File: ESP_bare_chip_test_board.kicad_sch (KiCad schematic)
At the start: 0 parts

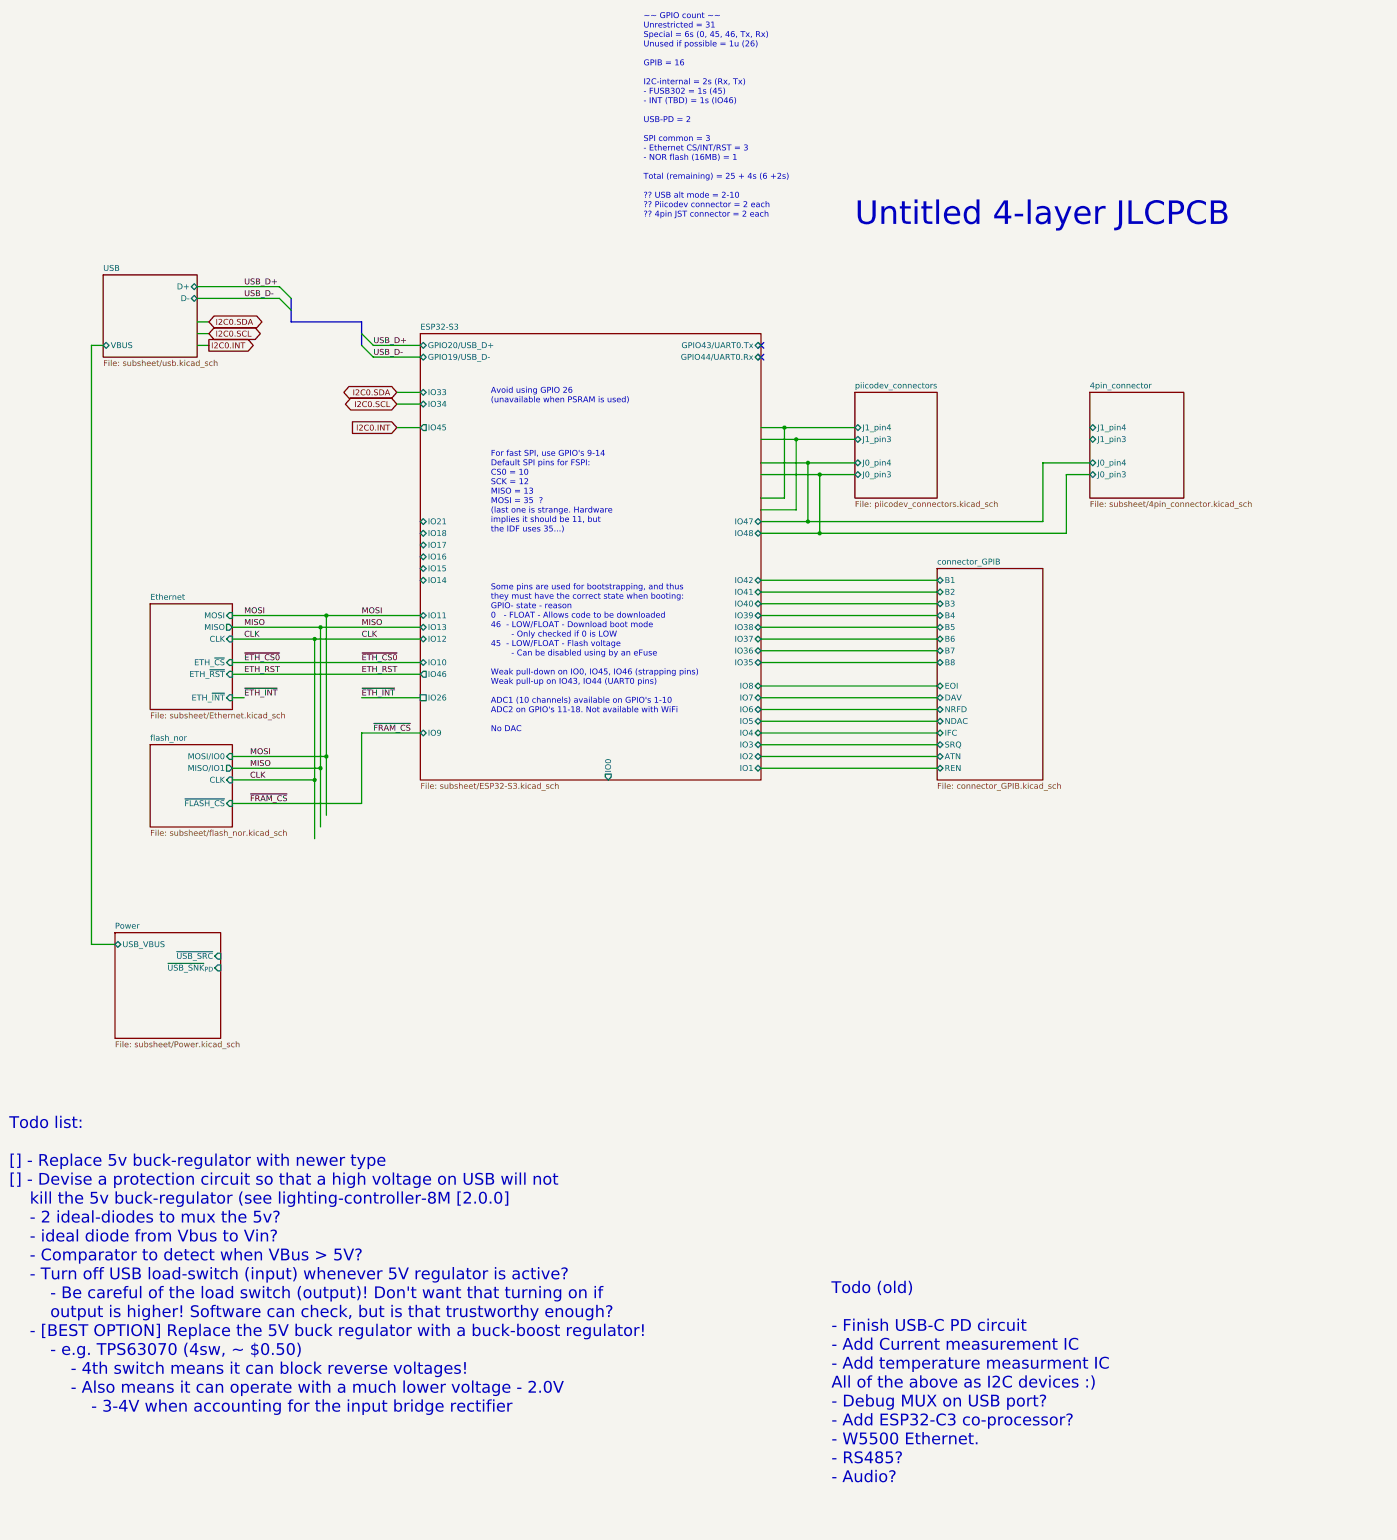
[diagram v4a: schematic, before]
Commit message: partial! Ran wires for GPIB connector
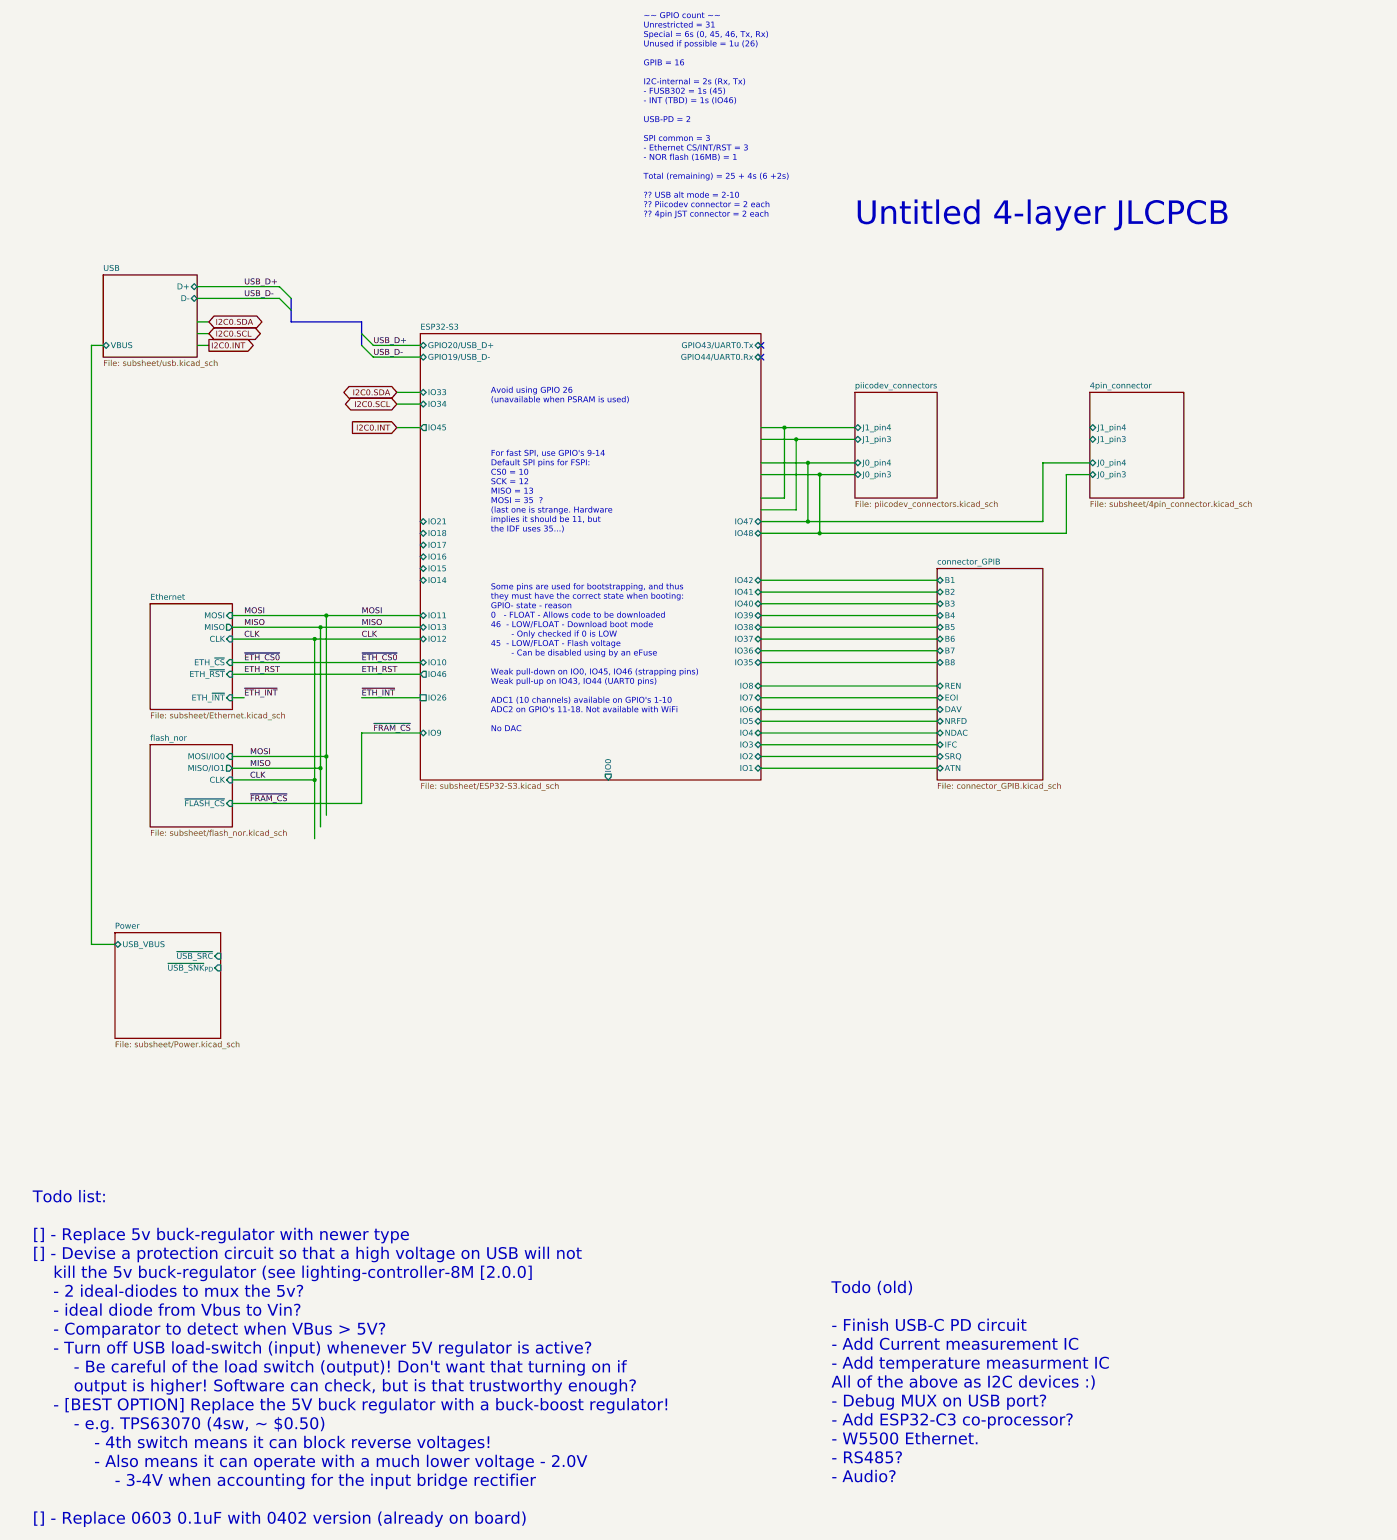
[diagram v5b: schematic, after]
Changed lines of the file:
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@@
 		)
 	)
-	(text "Todo list:\n\n[] - Replace 5v buck-regulator with newer type\n[] - Devise a protection circuit so that a high voltage on USB will not\n	kill the 5v buck-regulator (see lighting-controller-8M [2.0.0]\n	- 2 ideal-diodes to mux the 5v?\n	- ideal diode from Vbus to Vin?\n	- Comparator to detect when VBus > 5V?\n	- Turn off USB load-switch (input) whenever 5V regulator is active?\n		- Be careful of the load switch (output)! Don't want that turning on if\n		output is higher! Software can check, but is that trustworthy enough?\n	- [BEST OPTION] Replace the 5V buck regulator with a buck-boost regulator!\n		- e.g. TPS63070 (4sw, ~ $0.50)\n			- 4th switch means it can block reverse voltages!\n			- Also means it can operate with a much lower voltage - 2.0V\n				- 3-4V when accounting for the input bridge rectifier"
+	(text "Todo list:\n\n[] - Replace 5v buck-regulator with newer type\n[] - Devise a protection circuit so that a high voltage on USB will not\n	kill the 5v buck-regulator (see lighting-controller-8M [2.0.0]\n	- 2 ideal-diodes to mux the 5v?\n	- ideal diode from Vbus to Vin?\n	- Comparator to detect when VBus > 5V?\n	- Turn off USB load-switch (input) whenever 5V regulator is active?\n		- Be careful of the load switch (output)! Don't want that turning on if\n		output is higher! Software can check, but is that trustworthy enough?\n	- [BEST OPTION] Replace the 5V buck regulator with a buck-boost regulator!\n		- e.g. TPS63070 (4sw, ~ $0.50)\n			- 4th switch means it can block reverse voltages!\n			- Also means it can operate with a much lower voltage - 2.0V\n				- 3-4V when accounting for the input bridge rectifier\n\n[] - Replace 0603 0.1uF with 0402 version (already on board)"
 		(exclude_from_sim no)
-		(at -2.54 264.16 0)
+		(at 2.54 215.9 0)
 		(effects
 			(font
 				(size 2.54 2.54)
 			)
-			(justify left bottom)
+			(justify left top)
 		)
 	)
@@
 		)
 		(pin "ATN" bidirectional
+			(at 198.12 124.46 180)
+			(effects
+				(font
+					(size 1.27 1.27)
+				)
+				(justify left)
+			)
+		)
+		(pin "NRFD" bidirectional
+			(at 198.12 114.3 180)
+			(effects
+				(font
+					(size 1.27 1.27)
+				)
+				(justify left)
+			)
+		)
+		(pin "IFC" bidirectional
+			(at 198.12 119.38 180)
+			(effects
+				(font
+					(size 1.27 1.27)
+				)
+				(justify left)
+			)
+		)
+		(pin "NDAC" bidirectional
+			(at 198.12 116.84 180)
+			(effects
+				(font
+					(size 1.27 1.27)
+				)
+				(justify left)
+			)
+		)
+		(pin "SRQ" bidirectional
 			(at 198.12 121.92 180)
 			(effects
@@
 			)
 		)
-		(pin "NRFD" bidirectional
+		(pin "EOI" bidirectional
+			(at 198.12 109.22 180)
+			(effects
+				(font
+					(size 1.27 1.27)
+				)
+				(justify left)
+			)
+		)
+		(pin "DAV" bidirectional
 			(at 198.12 111.76 180)
 			(effects
@@
 			)
 		)
-		(pin "IFC" bidirectional
-			(at 198.12 116.84 180)
-			(effects
-				(font
-					(size 1.27 1.27)
-				)
-				(justify left)
-			)
-		)
-		(pin "NDAC" bidirectional
-			(at 198.12 114.3 180)
-			(effects
-				(font
-					(size 1.27 1.27)
-				)
-				(justify left)
-			)
-		)
-		(pin "SRQ" bidirectional
-			(at 198.12 119.38 180)
-			(effects
-				(font
-					(size 1.27 1.27)
-				)
-				(justify left)
-			)
-		)
-		(pin "EOI" bidirectional
+		(pin "REN" bidirectional
 			(at 198.12 106.68 180)
 			(effects
 				(font
-					(size 1.27 1.27)
-				)
-				(justify left)
-			)
-		)
-		(pin "DAV" bidirectional
-			(at 198.12 109.22 180)
-			(effects
-				(font
-					(size 1.27 1.27)
-				)
-				(justify left)
-			)
-		)
-		(pin "REN" bidirectional
-			(at 198.12 124.46 180)
-			(effects
-				(font

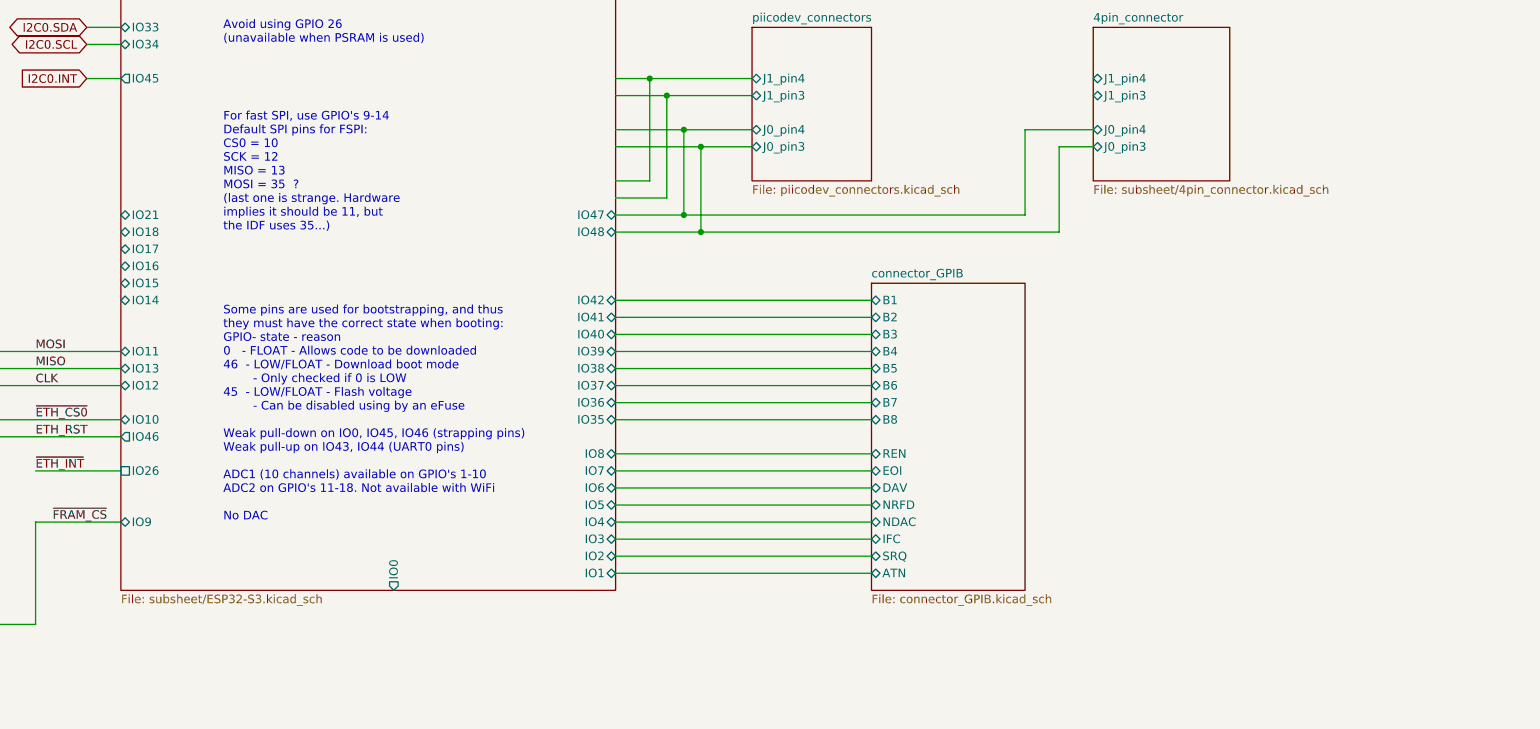
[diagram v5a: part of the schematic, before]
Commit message: Position final few components
Removed one ESD diode arrray - experimental board, so not really needed,
with the exception of the USB lines.

Add and position 5V indicator LED

Finished wiring up the 5V buck-boost regulator
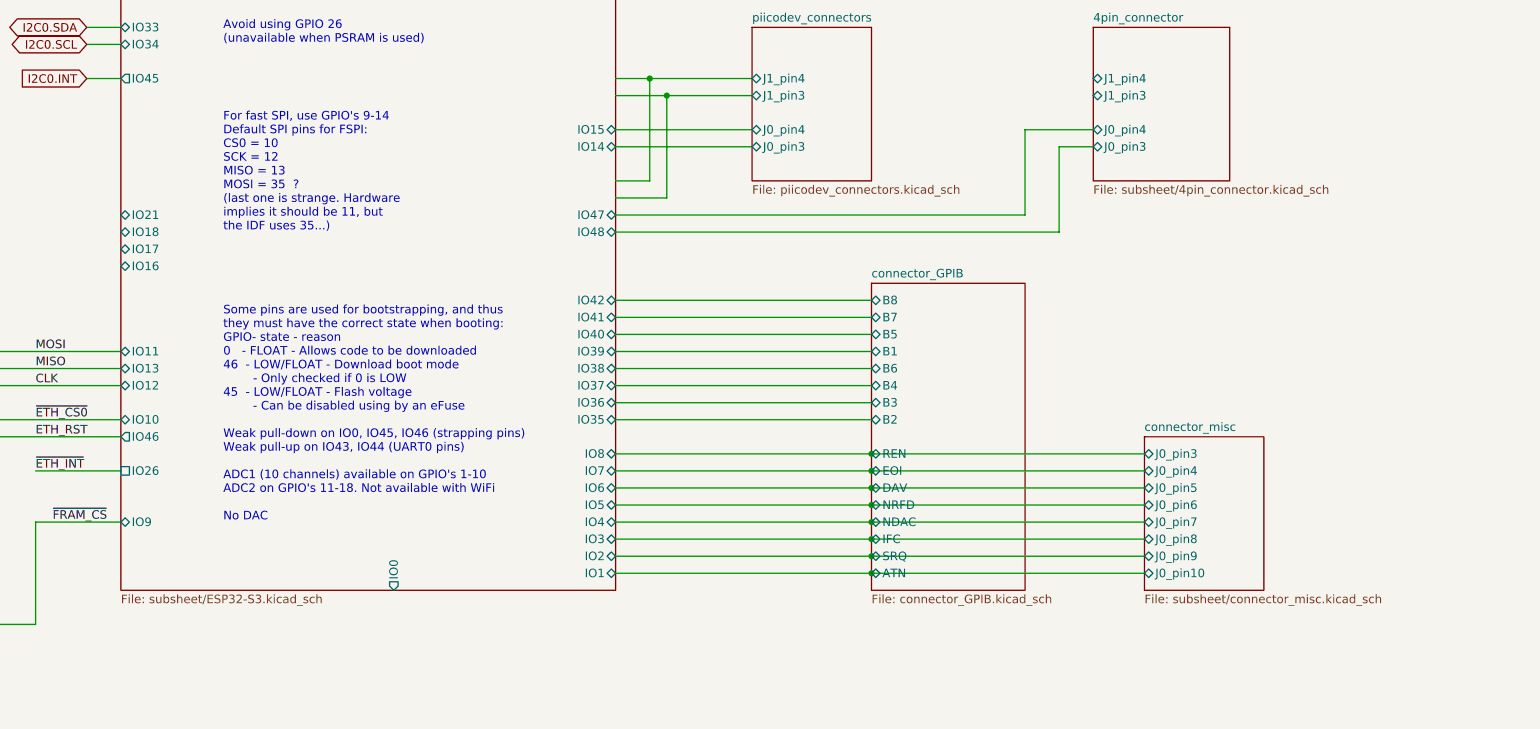
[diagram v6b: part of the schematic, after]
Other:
- added sheet connector_misc (subsheet/connector_misc.kicad_sch)
